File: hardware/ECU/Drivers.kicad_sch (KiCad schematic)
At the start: 36 parts, among them Q4 IRFB4110PBF, Q5 IRFB4110PBF, Q6 IRFB4110PBF, Q7 IRFB4110PBF, SW4 SW_DPDT_x2, U5 TC4424A, U7 MC33810, U9 TC4424A

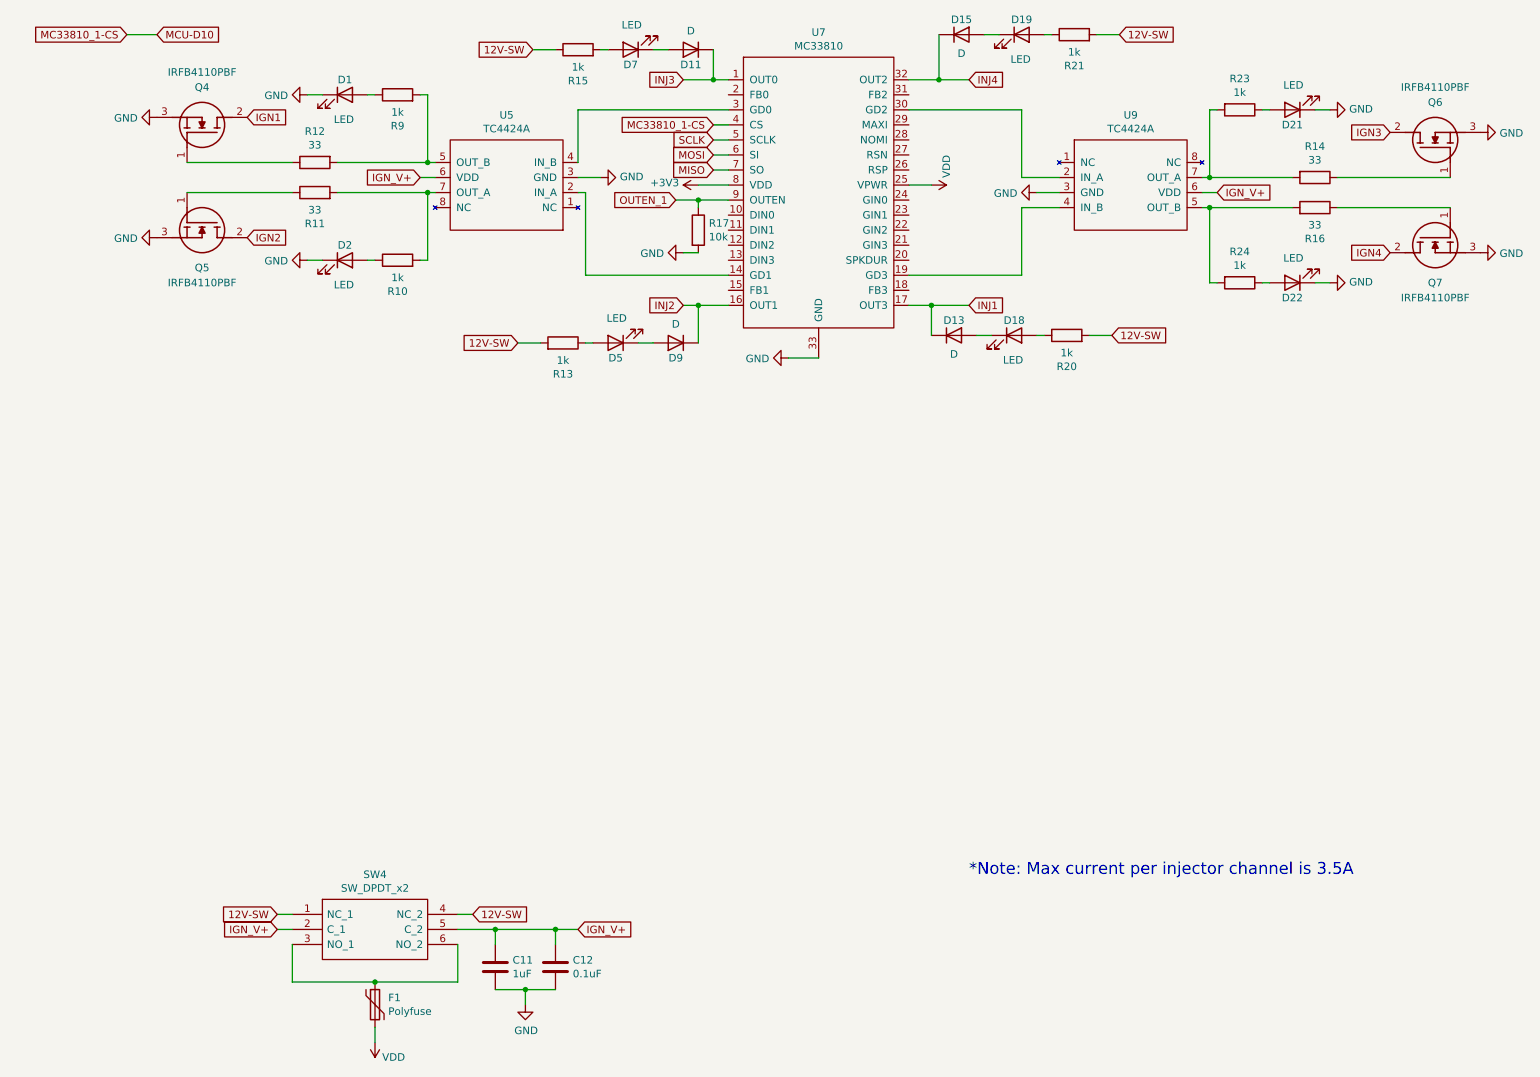
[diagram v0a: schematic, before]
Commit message: Replace speeduino submodule with HasiKe fork, fix teensy.pretty path
- Switch speeduino from speeduino/speeduino to HasiKe/speeduino
- Fix teensy.pretty submodule path case mismatch (Hardware -> hardware)
- Add ISL9V5036P3-F085 component library
- Various ECU schematic updates
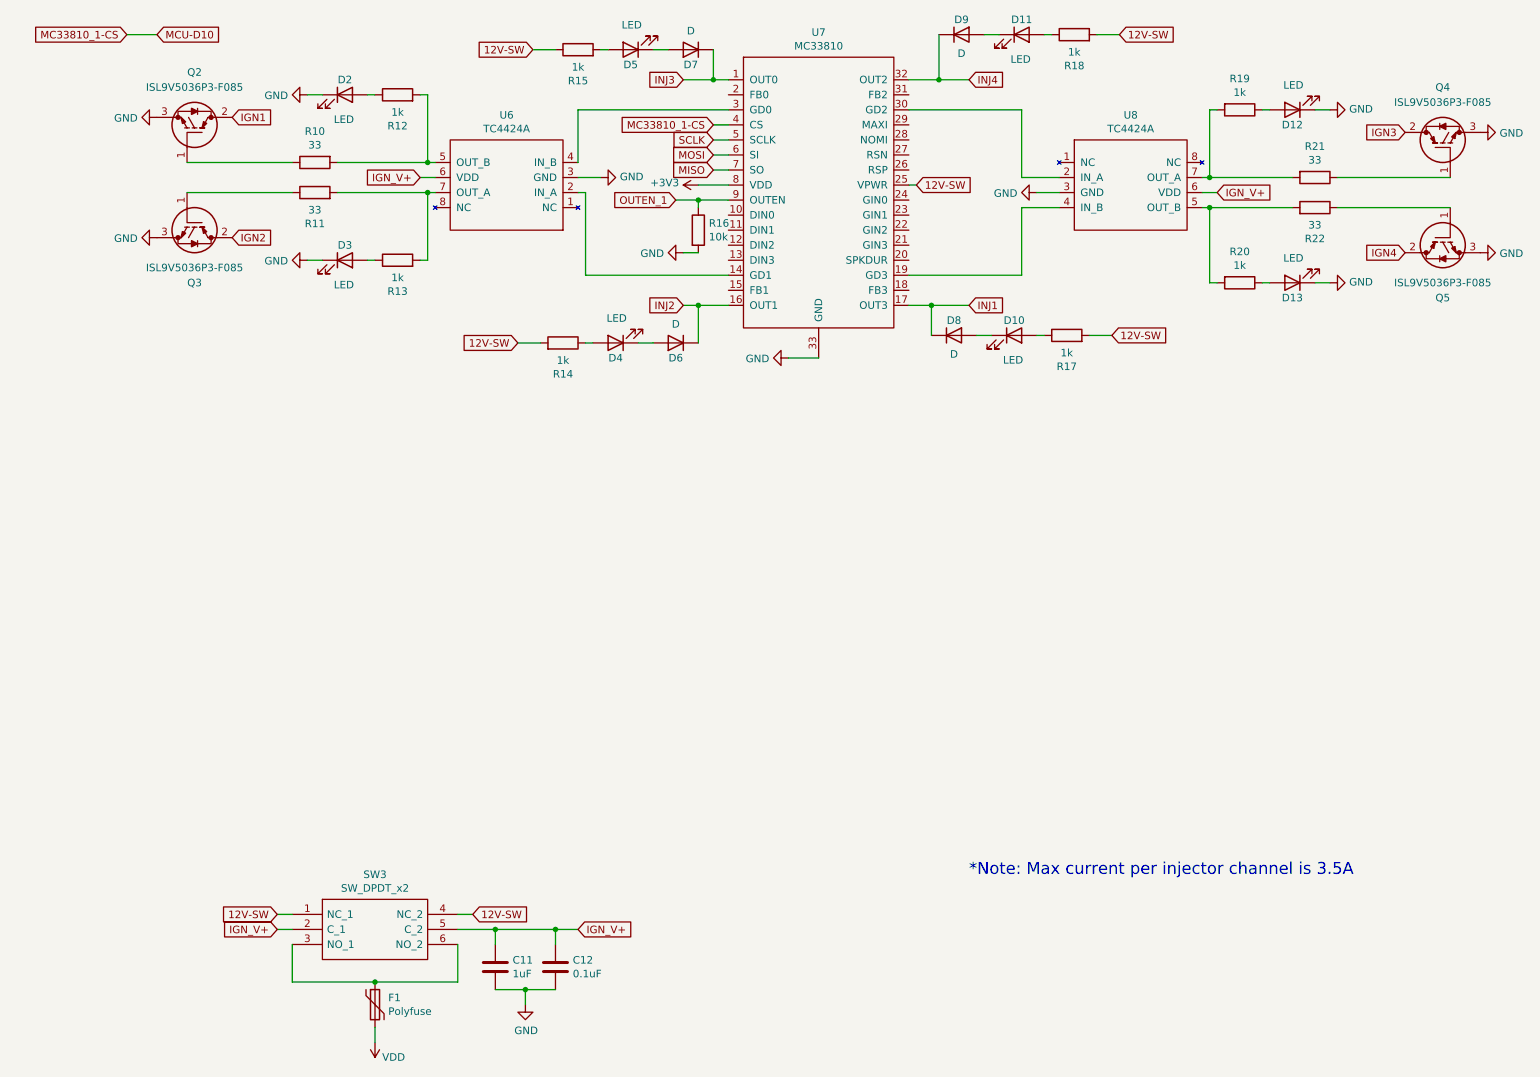
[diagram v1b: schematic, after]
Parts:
- removed Q4, Q5, Q6, Q7: IRFB4110PBF, TO254P483X1016X1994-3P, symbol LIB_IRFB4110PBF:IRFB4110PBF
- added Q2, Q3, Q4, Q5: ISL9V5036P3-F085, TO254P470X1016X2019-3P, symbol ISL9V5036P3-F085:ISL9V5036P3-F085
- renumbered D18 to D10, D19 to D11, D21 to D12, D22 to D13, D1 to D2, D2 to D3, D5 to D4, D7 to D5, D9 to D6, D11 to D7, D13 to D8, D15 to D9, R12 to R10, R9 to R12, R10 to R13, R13 to R14, R17 to R16, R20 to R17, R21 to R18, R23 to R19, R24 to R20, R14 to R21, R16 to R22, SW4 to SW3, U5 to U6, U9 to U8
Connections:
- net 12V-SW: now also U7.25 (VPWR)
- net GND: now also Q2.3, Q3.3, Q4.3, Q5.3
- net IGN1: now also Q2.2
- net IGN2: now also Q3.2
- net IGN3: now also Q4.2
- net IGN4: now also Q5.2
- net VDD: no longer U7.25 (VPWR)
- net at R11.1: now also Q3.1
- net at R22.1: now also Q5.1
- net at R10.1: now also Q2.1
- net at R21.1: now also Q4.1
